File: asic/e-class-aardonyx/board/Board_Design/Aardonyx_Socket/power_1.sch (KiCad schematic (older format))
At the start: 29 parts, among them J5 PJ-202H PWRJACK, J6 Conn_1x3_M, SW1 SW_SPST, U4 TPS54627DDAR

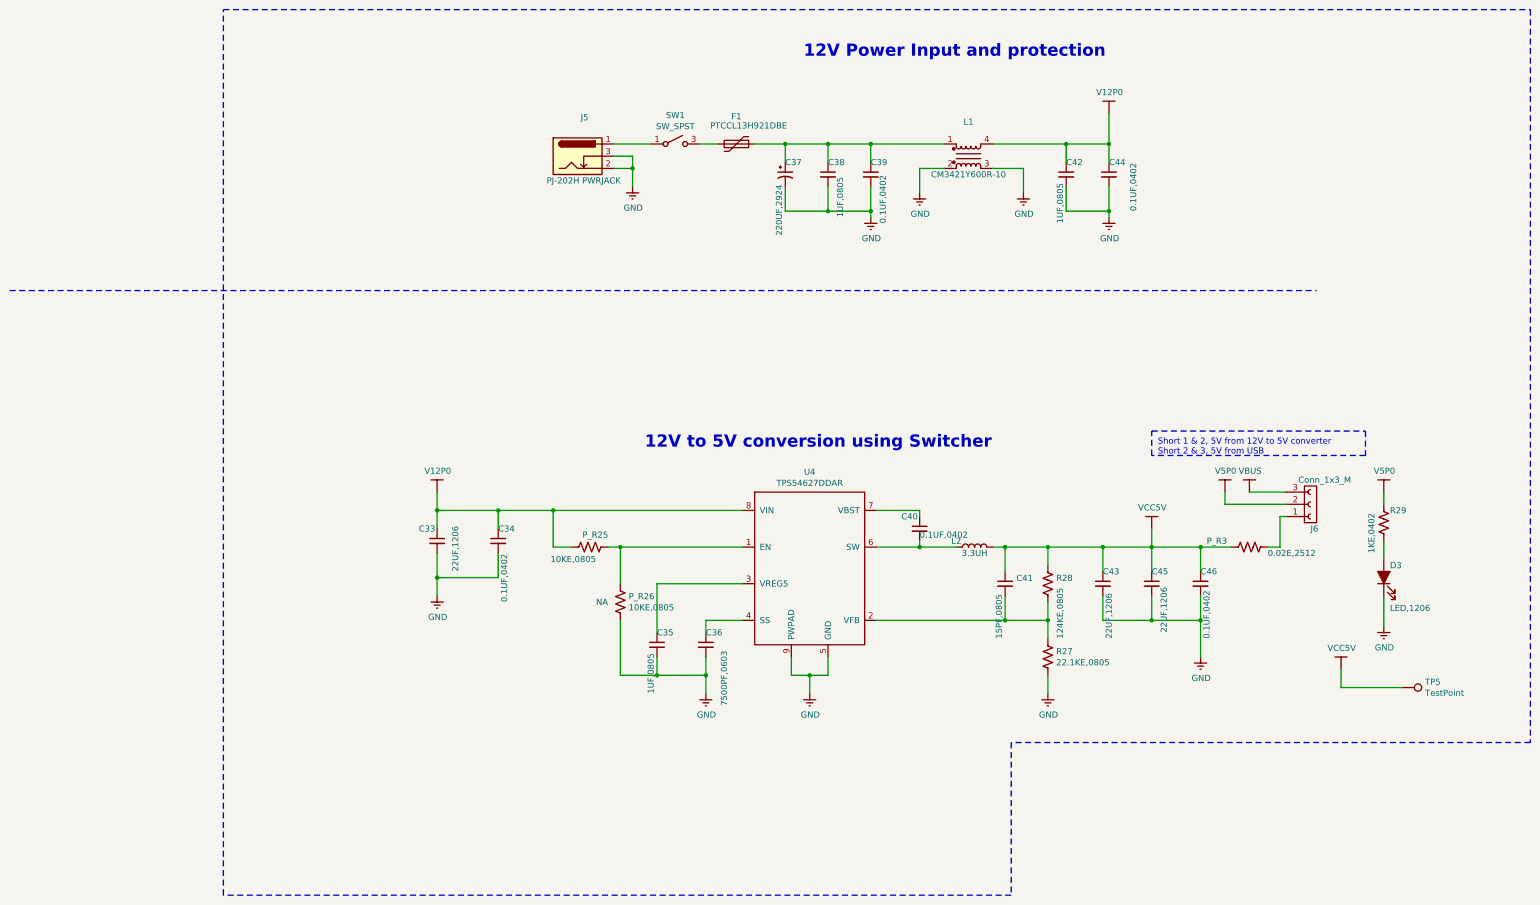
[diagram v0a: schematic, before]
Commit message: update socket compo placement
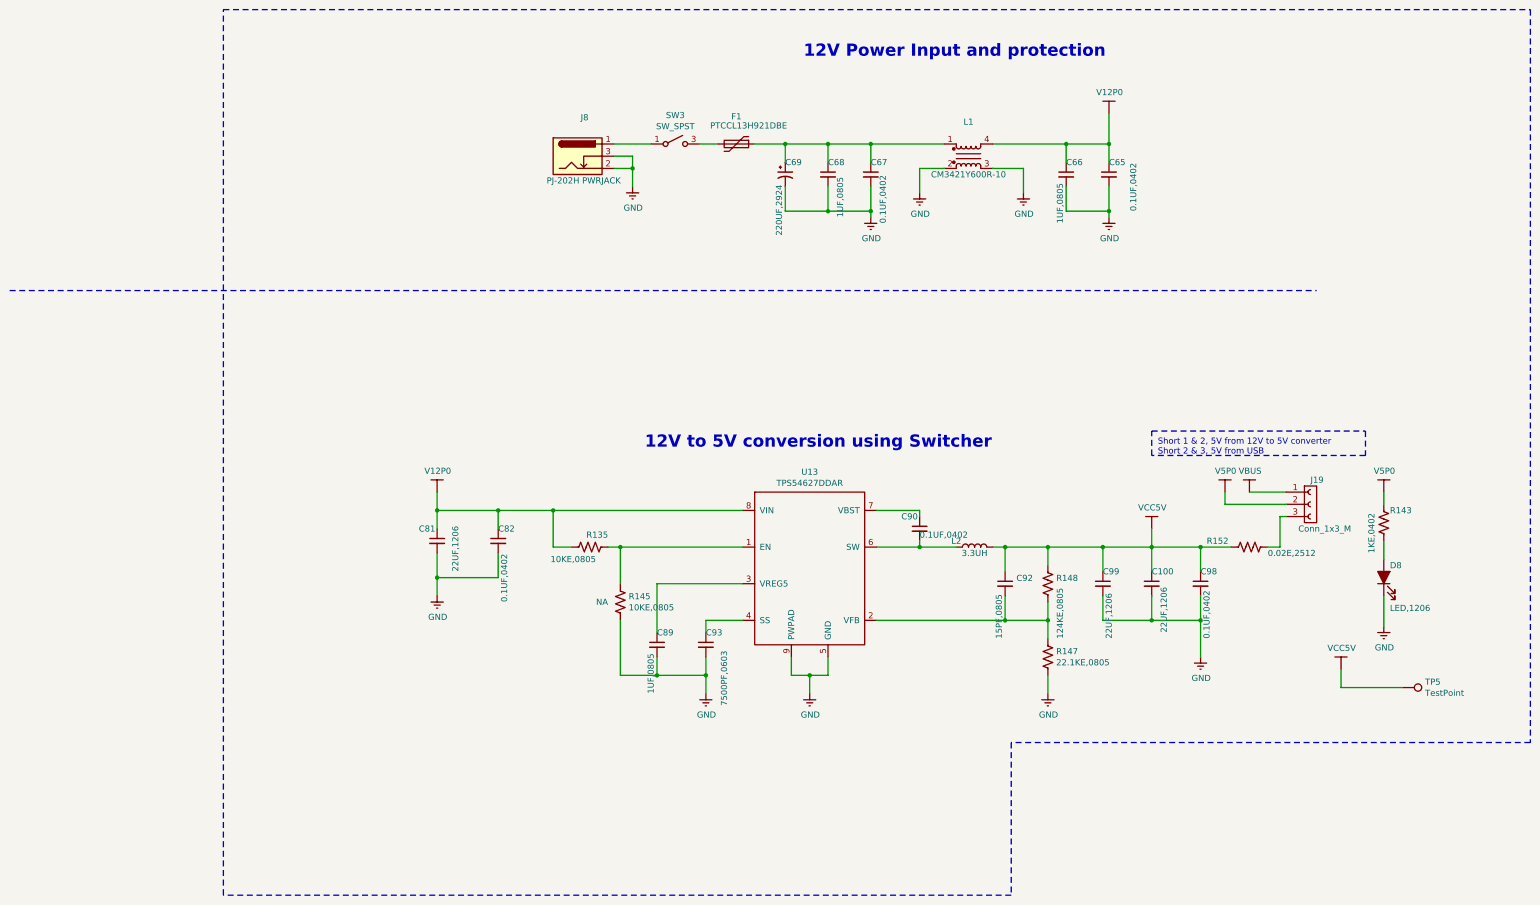
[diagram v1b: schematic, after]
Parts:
- C69: renamed from C37; footprint Aardonyx:CP_EIA-7260-38_VISHAY_Pad2.68x7.50mm_HandSolder -> Aardonyx:CP_EIA-2924_tcn4227_Pad6.1x7.3mm
- F1: footprint Aardonyx:vishay_ptccl_d1mm_w5mm -> Aardonyx:vishay_ptccl_d12.5mm_w4mm
- J8: renamed from J5; footprint Aardonyx:Pwr_Jack_DC_PJ-202AH_Horizontal -> Aardonyx:CUI_PJ-202AH
- renumbered C45 to C100, C44 to C65, C42 to C66, C39 to C67, C38 to C68, C33 to C81, C34 to C82, C35 to C89, C40 to C90, C41 to C92, C36 to C93, C46 to C98, C43 to C99, D3 to D8, J6 to J19, P_R25 to R135, R29 to R143, P_R26 to R145, R27 to R147, R28 to R148, P_R3 to R152, SW1 to SW3, U4 to U13
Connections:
- net VBUS: now also J19.1 (Pin_1); no longer J19.3 (Pin_3)
- net at R152.1: now also J19.3 (Pin_3); no longer J19.1 (Pin_1)

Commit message: Back annotation
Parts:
- renumbered C65 to C63, C66 to C64, C67 to C65, C68 to C66, C69 to C67, C81 to C70, C82 to C78, C89 to C79, C90 to C80, C92 to C81, C93 to C82, J8 to J10, R135 to R127, R143 to R135, R145 to R137, R147 to R138, R148 to R139, R152 to R151
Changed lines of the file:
@@
 	6900 5500 6900 5300
 $Comp
-L Aardonyx-rescue:C_Small-aardonyx C92
+L Aardonyx-rescue:C_Small-aardonyx C81
 U 1 1 5DC0C5AC
 P 6900 5200
-AR Path="/5DB8A7DC/5DC0C5AC" Ref="C92"  Part="1"
+AR Path="/5DB8A7DC/5DC0C5AC" Ref="C81"  Part="1"
 AR Path="/5E6E93B2/5DC0C5AC" Ref="C?"  Part="1"
-F 0 "C92" H 6992 5246 50  0000 L CNN
+F 0 "C81" H 6992 5246 50  0000 L CNN
 F 1 "15PF,0805" V 6850 4750 50  0000 L CNN
 F 2 "Capacitor_SMD:C_0805_2012Metric" H 6900 5200 50  0001 C CNN
@@
 	5850 4600 6200 4600
 $Comp
-L Aardonyx-rescue:C_Small-aardonyx C90
+L Aardonyx-rescue:C_Small-aardonyx C80
 U 1 1 5DC07BC9
 P 6200 4750
-AR Path="/5DB8A7DC/5DC07BC9" Ref="C90"  Part="1"
+AR Path="/5DB8A7DC/5DC07BC9" Ref="C80"  Part="1"
 AR Path="/5E6E93B2/5DC07BC9" Ref="C?"  Part="1"
-F 0 "C90" H 6050 4850 50  0000 L CNN
+F 0 "C80" H 6050 4850 50  0000 L CNN
 F 1 "0.1UF,0402" H 6200 4700 50  0000 L CNN
 F 2 "Capacitor_SMD:C_0402_1005Metric" H 6200 4750 50  0001 C CNN
@@
 	2250 4600 2250 4750
 $Comp
-L Aardonyx-rescue:C_Small-aardonyx C81
+L Aardonyx-rescue:C_Small-aardonyx C70
 U 1 1 5DC04203
 P 2250 4850
-AR Path="/5DB8A7DC/5DC04203" Ref="C81"  Part="1"
+AR Path="/5DB8A7DC/5DC04203" Ref="C70"  Part="1"
 AR Path="/5E6E93B2/5DC04203" Ref="C?"  Part="1"
-F 0 "C81" H 2100 4950 50  0000 L CNN
+F 0 "C70" H 2100 4950 50  0000 L CNN
 F 1 "22UF,1206" V 2400 4600 50  0000 L CNN
 F 2 "Capacitor_SMD:C_1206_3216Metric" H 2250 4850 50  0001 C CNN
@@
 $EndComp
 $Comp
-L Aardonyx-rescue:C_Small-aardonyx C82
+L Aardonyx-rescue:C_Small-aardonyx C78
 U 1 1 5DC03EB5
 P 2750 4850
-AR Path="/5DB8A7DC/5DC03EB5" Ref="C82"  Part="1"
+AR Path="/5DB8A7DC/5DC03EB5" Ref="C78"  Part="1"
 AR Path="/5E6E93B2/5DC03EB5" Ref="C?"  Part="1"
-F 0 "C82" H 2750 4950 50  0000 L CNN
+F 0 "C78" H 2750 4950 50  0000 L CNN
 F 1 "0.1UF,0402" V 2800 4350 50  0000 L CNN
 F 2 "Capacitor_SMD:C_0402_1005Metric" H 2750 4850 50  0001 C CNN
@@
 	3650 4900 3750 4900
 $Comp
-L Aardonyx-rescue:R_US-aardonyx R135
+L Aardonyx-rescue:R_US-aardonyx R127
 U 1 1 5DC02AA4
 P 3500 4900
-AR Path="/5DB8A7DC/5DC02AA4" Ref="R135"  Part="1"
+AR Path="/5DB8A7DC/5DC02AA4" Ref="R127"  Part="1"
 AR Path="/5E6E93B2/5DC02AA4" Ref="R?"  Part="1"
-F 0 "R135" V 3600 4750 50  0000 L CNN
+F 0 "R127" V 3600 4750 50  0000 L CNN
 F 1 "10KE,0805" V 3400 4850 50  0000 L CNN
 F 2 "Resistor_SMD:R_0805_2012Metric" V 3540 4890 50  0001 C CNN
@@
 	3750 4900 4750 4900
 $Comp
-L Aardonyx-rescue:R_US-aardonyx R145
+L Aardonyx-rescue:R_US-aardonyx R137
 U 1 1 5DC003B9
 P 3750 5350
-AR Path="/5DB8A7DC/5DC003B9" Ref="R145"  Part="1"
+AR Path="/5DB8A7DC/5DC003B9" Ref="R137"  Part="1"
 AR Path="/5E6E93B2/5DC003B9" Ref="R?"  Part="1"
-F 0 "R145" H 3818 5396 50  0000 L CNN
+F 0 "R137" H 3818 5396 50  0000 L CNN
 F 1 "10KE,0805" H 3818 5305 50  0000 L CNN
 F 2 "Resistor_SMD:R_0805_2012Metric" V 3790 5340 50  0001 C CNN
@@
 $EndComp
 $Comp
-L Aardonyx-rescue:C_Small-aardonyx C89
+L Aardonyx-rescue:C_Small-aardonyx C79
 U 1 1 5DBFC886
 P 4050 5700
-AR Path="/5DB8A7DC/5DBFC886" Ref="C89"  Part="1"
+AR Path="/5DB8A7DC/5DBFC886" Ref="C79"  Part="1"
 AR Path="/5E6E93B2/5DBFC886" Ref="C?"  Part="1"
-F 0 "C89" H 4050 5800 50  0000 L CNN
+F 0 "C79" H 4050 5800 50  0000 L CNN
 F 1 "1UF,0805" V 4000 5300 50  0000 L CNN
 F 2 "Capacitor_SMD:C_0805_2012Metric" H 4050 5700 50  0001 C CNN
@@
 	4050 5200 4750 5200
 $Comp
-L Aardonyx-rescue:C_Small-aardonyx C93
+L Aardonyx-rescue:C_Small-aardonyx C82
 U 1 1 5DBFC58F
 P 4450 5700
-AR Path="/5DB8A7DC/5DBFC58F" Ref="C93"  Part="1"
+AR Path="/5DB8A7DC/5DBFC58F" Ref="C82"  Part="1"
 AR Path="/5E6E93B2/5DBFC58F" Ref="C?"  Part="1"
-F 0 "C93" H 4450 5800 50  0000 L CNN
+F 0 "C82" H 4450 5800 50  0000 L CNN
 F 1 "7500PF,0603" V 4600 5200 50  0000 L CNN
 F 2 "Capacitor_SMD:C_0603_1608Metric" H 4450 5700 50  0001 C CNN
@@
 	5450 2150 5450 1950
 $Comp
-L Aardonyx-rescue:C_Small-aardonyx C68
+L Aardonyx-rescue:C_Small-aardonyx C66
 U 1 1 5E824D85
 P 5450 1850
-AR Path="/5DB8A7DC/5E824D85" Ref="C68"  Part="1"
+AR Path="/5DB8A7DC/5E824D85" Ref="C66"  Part="1"
 AR Path="/5E6E93B2/5E824D85" Ref="C?"  Part="1"
-F 0 "C68" H 5450 1950 50  0000 L CNN
+F 0 "C66" H 5450 1950 50  0000 L CNN
 F 1 "1UF,0805" V 5550 1500 50  0000 L CNN
 F 2 "Capacitor_SMD:C_0805_2012Metric" H 5450 1850 50  0001 C CNN
@@
 $EndComp
 $Comp
-L Aardonyx-rescue:C_Small-aardonyx C67
+L Aardonyx-rescue:C_Small-aardonyx C65
 U 1 1 5E8299D0
 P 5800 1850
-AR Path="/5DB8A7DC/5E8299D0" Ref="C67"  Part="1"
+AR Path="/5DB8A7DC/5E8299D0" Ref="C65"  Part="1"
 AR Path="/5E6E93B2/5E8299D0" Ref="C?"  Part="1"
-F 0 "C67" H 5800 1950 50  0000 L CNN
+F 0 "C65" H 5800 1950 50  0000 L CNN
 F 1 "0.1UF,0402" V 5900 1450 50  0000 L CNN
 F 2 "Capacitor_SMD:C_0402_1005Metric" H 5800 1850 50  0001 C CNN
@@
 	9150 4650 9200 4650
 $Comp
-L Device:CP1_Small C69
+L Device:CP1_Small C67
 U 1 1 5E53A053
 P 5100 1850
-AR Path="/5DB8A7DC/5E53A053" Ref="C69"  Part="1"
+AR Path="/5DB8A7DC/5E53A053" Ref="C67"  Part="1"
 AR Path="/5E6E93B2/5E53A053" Ref="C?"  Part="1"
-F 0 "C69" H 5100 1950 50  0000 L CNN
+F 0 "C67" H 5100 1950 50  0000 L CNN
 F 1 "220UF,2924" V 5050 1350 50  0000 L CNN
 F 2 "Aardonyx:CP_EIA-2924_tcn4227_Pad6.1x7.3mm" H 5100 1850 50  0001 C CNN
@@
 	7400 2150 7400 1950
 $Comp
-L Aardonyx-rescue:C_Small-aardonyx C66
+L Aardonyx-rescue:C_Small-aardonyx C64
 U 1 1 5E5FEAFA
 P 7400 1850
-AR Path="/5DB8A7DC/5E5FEAFA" Ref="C66"  Part="1"
+AR Path="/5DB8A7DC/5E5FEAFA" Ref="C64"  Part="1"
 AR Path="/5E6E93B2/5E5FEAFA" Ref="C?"  Part="1"
-F 0 "C66" H 7400 1950 50  0000 L CNN
+F 0 "C64" H 7400 1950 50  0000 L CNN
 F 1 "1UF,0805" V 7350 1450 50  0000 L CNN
 F 2 "Capacitor_SMD:C_0805_2012Metric" H 7400 1850 50  0001 C CNN
@@
 $EndComp
 $Comp
-L Aardonyx-rescue:C_Small-aardonyx C65
+L Aardonyx-rescue:C_Small-aardonyx C63
 U 1 1 5E5FEB00
 P 7750 1850
-AR Path="/5DB8A7DC/5E5FEB00" Ref="C65"  Part="1"
+AR Path="/5DB8A7DC/5E5FEB00" Ref="C63"  Part="1"
 AR Path="/5E6E93B2/5E5FEB00" Ref="C?"  Part="1"
-F 0 "C65" H 7750 1950 50  0000 L CNN
+F 0 "C63" H 7750 1950 50  0000 L CNN
 F 1 "0.1UF,0402" V 7950 1550 50  0000 L CNN
 F 2 "Capacitor_SMD:C_0402_1005Metric" H 7750 1850 50  0001 C CNN
@@
 $EndComp
 $Comp
-L Aardonyx-rescue:R_US-aardonyx R143
+L Aardonyx-rescue:R_US-aardonyx R135
 U 1 1 5E6A34B8
 P 10000 4700
-AR Path="/5DB8A7DC/5E6A34B8" Ref="R143"  Part="1"
+AR Path="/5DB8A7DC/5E6A34B8" Ref="R135"  Part="1"
 AR Path="/5E6E93B2/5E6A34B8" Ref="R?"  Part="1"
-F 0 "R143" H 10050 4800 50  0000 L CNN
+F 0 "R135" H 10050 4800 50  0000 L CNN
 F 1 "1KE,0402" V 9900 4450 50  0000 L CNN
 F 2 "Resistor_SMD:R_0402_1005Metric" V 10040 4690 50  0001 C CNN
@@
 	7750 1350 7750 1600
 $Comp
-L Aardonyx-rescue:R_US-aardonyx R148
+L Aardonyx-rescue:R_US-aardonyx R139
 U 1 1 5DC0E17E
 P 7250 5200
-AR Path="/5DB8A7DC/5DC0E17E" Ref="R148"  Part="1"
+AR Path="/5DB8A7DC/5DC0E17E" Ref="R139"  Part="1"
 AR Path="/5E6E93B2/5DC0E17E" Ref="R?"  Part="1"
-F 0 "R148" H 7318 5246 50  0000 L CNN
+F 0 "R139" H 7318 5246 50  0000 L CNN
 F 1 "124KE,0805" V 7350 4750 50  0000 L CNN
 F 2 "Resistor_SMD:R_0805_2012Metric" V 7290 5190 50  0001 C CNN
@@
 	10000 5300 10000 5550
 $Comp
-L Aardonyx-rescue:R_US-skt32e_asic R147
+L Aardonyx-rescue:R_US-skt32e_asic R138
 U 1 1 5EE2D8E4
 P 7250 5800
-F 0 "R147" H 7318 5846 50  0000 L CNN
+F 0 "R138" H 7318 5846 50  0000 L CNN
 F 1 "22.1KE,0805" H 7318 5755 50  0000 L CNN
 F 2 "Resistor_SMD:R_0805_2012Metric" V 7290 5790 50  0001 C CNN
@@
 $EndComp
 $Comp
-L Connector:Barrel_Jack_Switch J8
+L Connector:Barrel_Jack_Switch J10
 U 1 1 5E9E6D33
 P 3400 1700
-F 0 "J8" H 3457 2017 50  0000 C CNN
+F 0 "J10" H 3457 2017 50  0000 C CNN
 F 1 "PJ-202H PWRJACK" H 3450 1500 50  0000 C CNN
 F 2 "Aardonyx:CUI_PJ-202AH" H 3450 1660 50  0001 C CNN
@@
 	8100 4150 8100 3950
 $Comp
-L Aardonyx-rescue:R_US-aardonyx R152
+L Aardonyx-rescue:R_US-aardonyx R151
 U 1 1 5EF6EBAD
 P 8900 4900
-AR Path="/5DB8A7DC/5EF6EBAD" Ref="R152"  Part="1"
+AR Path="/5DB8A7DC/5EF6EBAD" Ref="R151"  Part="1"
 AR Path="/5E6E93B2/5EF6EBAD" Ref="P_R?"  Part="1"
-F 0 "R152" V 8850 4550 50  0000 L CNN
+F 0 "R151" V 8850 4550 50  0000 L CNN
 F 1 "0.02E,2512" V 8950 5050 50  0000 L CNN
 F 2 "Resistor_SMD:R_2512_6332Metric" V 8940 4890 50  0001 C CNN
